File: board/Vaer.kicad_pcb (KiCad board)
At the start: 2 copper layers, 84.4 x 84.4 mm, 36 parts, among them J1 USB_C_Receptacle, U1 ESP32-S3-WROOM-1, U2 NCP1117-3.3_SOT223, U3 BQ24073RGT, U4 BME280

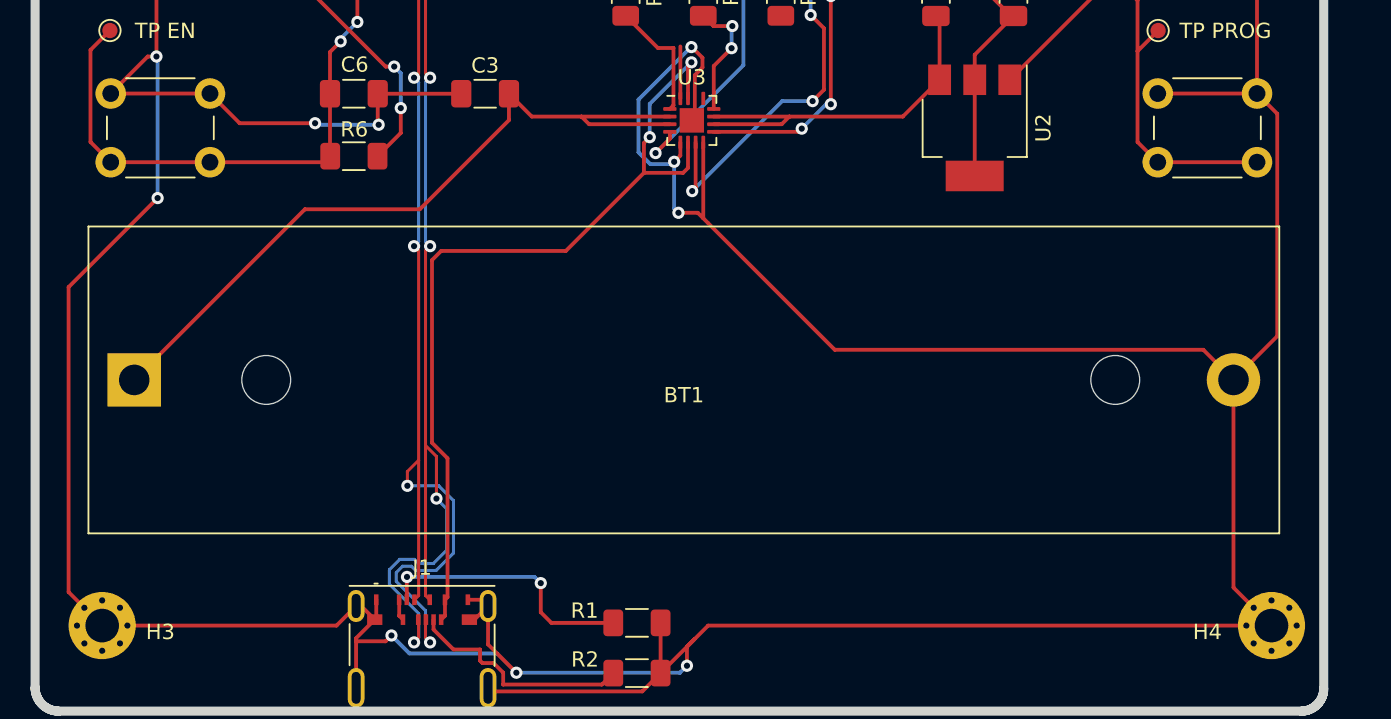
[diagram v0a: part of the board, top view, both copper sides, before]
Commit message: :recycle: Change the battery holder
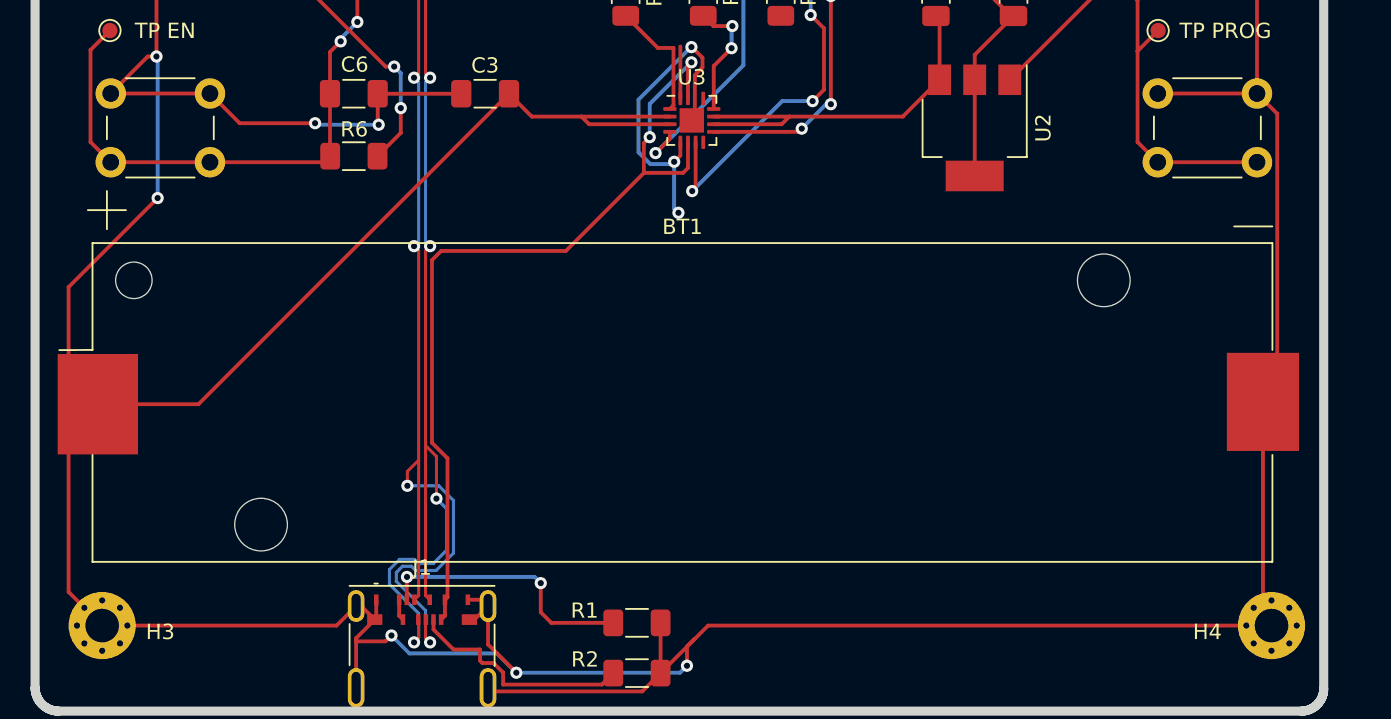
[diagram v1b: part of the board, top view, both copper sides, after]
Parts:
- BT1: footprint Battery:BatteryHolder_MPD_BH-18650-PC2 -> Battery:BatteryHolder_Keystone_1042_1x18650
- moved BT1 35.9 mm to (146.0, 113.2)
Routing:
- net GND: track 538.7 -> 491.2 mm
- net Net-(BT1-+): track 50.5 -> 52.5 mm

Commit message: :beers: Add code laying around locally :/
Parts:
- H1, H4: footprint MountingHole:MountingHole_2.2mm_M2_Pad_Via -> MountingHole:MountingHole_2.5mm_Pad_Via
- moved U4 183.8 mm to (282.9, 159.2)
- moved TP6 181.0 mm to (274.2, 161.7)
- moved TP1 174.3 mm to (268.1, 158.6)
- moved TP2 173.4 mm to (268.1, 161.7)
- moved TP3 171.8 mm to (271.1, 158.6)
- moved TP4 170.9 mm to (271.1, 161.7)
- moved C1 151.5 mm to (234.8, 158.8)
- moved SW_RESET1 151.1 mm to (239.8, 167.7)
- moved C2 150.5 mm to (234.8, 162.1)
- moved U3 146.9 mm to (278.3, 159.7)
- moved C6 137.8 mm to (234.8, 175.5), turned to 0 degrees
- moved D3 135.5 mm to (257.9, 176.1), turned to 0 degrees
- moved D2 128.7 mm to (257.9, 172.7), turned to 0 degrees
- moved U2 128.4 mm to (259.8, 181.9), turned to 0 degrees
- moved C3 124.9 mm to (234.8, 165.5)
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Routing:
- net GND: track 491.2 -> 0.00 mm, vias 10 -> 0
- net VCC_ESP: track 161.7 -> 0.00 mm, vias 8 -> 0
- net D+: track 80.6 -> 0.00 mm, vias 4 -> 0
- net D-: track 80.0 -> 0.64 mm, vias 6 -> 0
- net EN: track 75.6 -> 0.00 mm, vias 2 -> 0
- net ~{CE}: track 61.1 -> 0.00 mm, vias 4 -> 0
- net VCC_EBUS: track 57.5 -> 0.00 mm, vias 2 -> 0
- net PROG: track 52.7 -> 0.00 mm, vias 4 -> 0
- net Net-(BT1-+): track 52.5 -> 0.00 mm
- net ~{CHG}: track 48.0 -> 0.00 mm, vias 6 -> 0
- net ~{PGOOD}: track 44.4 -> 0.00 mm, vias 4 -> 0
- net MISO: track 41.8 -> 0.00 mm, vias 4 -> 0
- net MOSI: track 36.8 -> 0.00 mm, vias 2 -> 0
- net SCLK: track 34.4 -> 0.00 mm, vias 2 -> 0
- net CS: track 32.3 -> 0.00 mm, vias 4 -> 0
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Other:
- board text removed: "Humidity Pressure Temperature"
- board text removed: "PWR"
- board text removed: "TP CLK"
- board text removed: "TP CS"
- board text removed: "TP EN"
- board text removed: "TP MISO"
- board text removed: "TP MOSI"
- board text removed: "TP PROG"
- board text removed: "locked"
- board text removed: "~{CHG}"
- board text removed: "~{PGOOD}"

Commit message: :construction: Layed out the PCB again
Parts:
- moved U2 175.5 mm to (123.3, 71.5)
- moved SW_RESET1 165.3 mm to (117.0, 57.0)
- moved C6 158.6 mm to (129.4, 57.0)
- moved U3 158.4 mm to (135.2, 92.0), turned to 90 degrees
- moved C5 157.7 mm to (109.4, 76.5), turned to 180 degrees
- moved C2 157.4 mm to (109.4, 67.0)
- moved C1 152.7 mm to (109.5, 71.5)
- moved U4 141.5 mm to (158.5, 91.7), turned to 90 degrees
- moved D1 137.4 mm to (165.0, 68.0)
- moved D2 137.0 mm to (165.0, 72.0)
- moved D3 136.6 mm to (165.0, 76.0)
- moved C4 129.9 mm to (130.1, 92.0), turned to -90 degrees
- moved SW_FLASH1 127.3 mm to (163.8, 57.0)
- moved R1 118.8 mm to (114.5, 85.5), turned to 180 degrees
- moved R8 118.8 mm to (135.1, 88.0), turned to 180 degrees
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
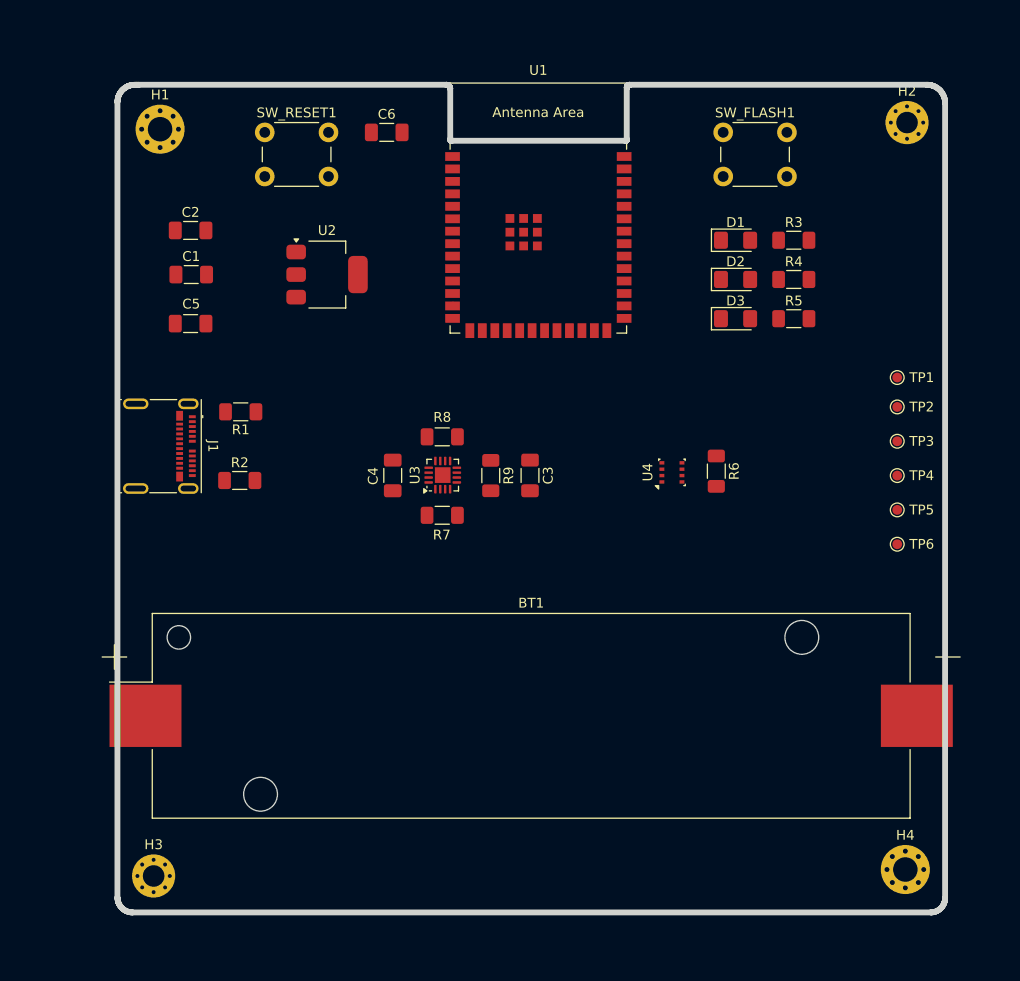
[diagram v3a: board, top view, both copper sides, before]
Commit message: :sparkles: Rerouted all components
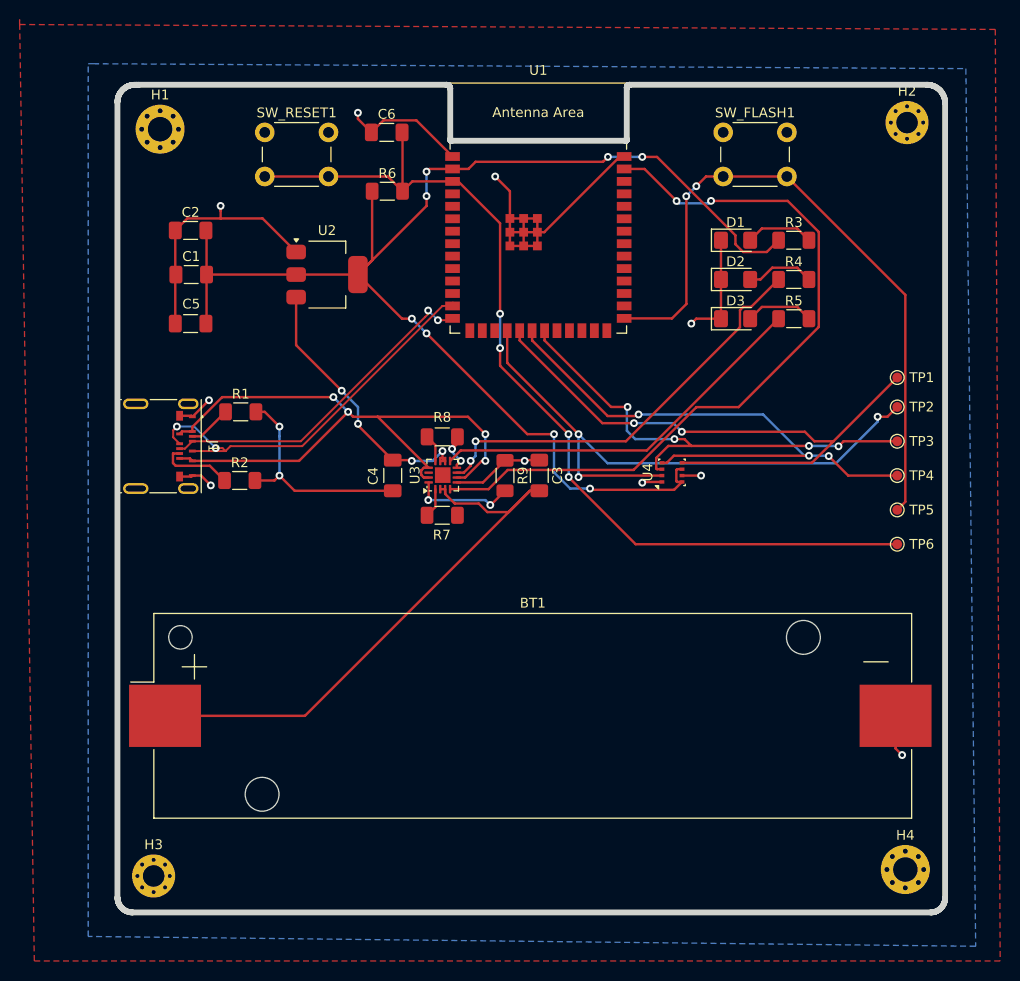
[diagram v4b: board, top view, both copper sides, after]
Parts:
- moved R6 44.1 mm to (129.5, 63.0), turned to 0 degrees
- moved R9 1.45 mm to (141.5, 92.0)
- moved C3 0.95 mm to (145.0, 92.0)
- moved BT1 0.16 mm to (144.3, 116.5)
- turned R1 to 0 degrees
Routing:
- net VCC_ESP: track 0.00 -> 136.3 mm, vias 0 -> 8
- net GND: track 0.00 -> 134.8 mm, vias 0 -> 14
- net EN: track 0.00 -> 98.0 mm, vias 0 -> 4
- net ~{CE}: track 0.00 -> 76.9 mm, vias 0 -> 2
- net VCC_EBUS: track 0.00 -> 69.8 mm, vias 0 -> 4
- net PROG: track 0.00 -> 68.4 mm, vias 0 -> 2
- net CS: track 0.00 -> 62.9 mm, vias 0 -> 3
- net MISO: track 0.00 -> 62.8 mm, vias 0 -> 2
- net SCLK: track 0.00 -> 59.4 mm, vias 0 -> 3
- net Net-(BT1-+): track 0.00 -> 59.0 mm
- net MOSI: track 0.00 -> 48.9 mm, vias 0 -> 4
- net ~{CHG}: track 0.00 -> 43.2 mm, vias 0 -> 2
- net D-: track 0.64 -> 41.5 mm, vias 0 -> 2
- net ~{PGOOD}: track 0.00 -> 39.5 mm
- net D+: track 0.00 -> 34.4 mm, vias 0 -> 2
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- added copper zone on F.Cu, net (none)
- added copper zone on B.Cu, net GND

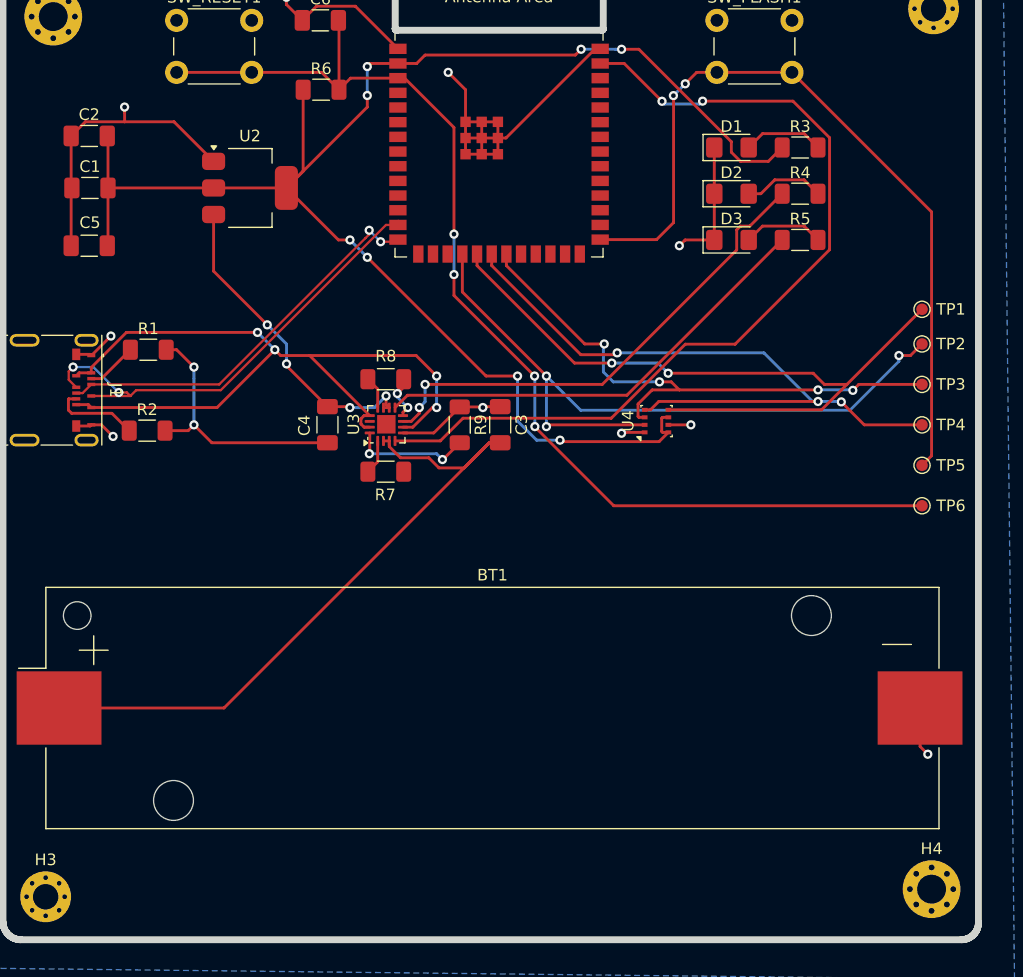
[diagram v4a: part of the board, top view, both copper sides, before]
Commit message: :sparkles: Add some missing board markings
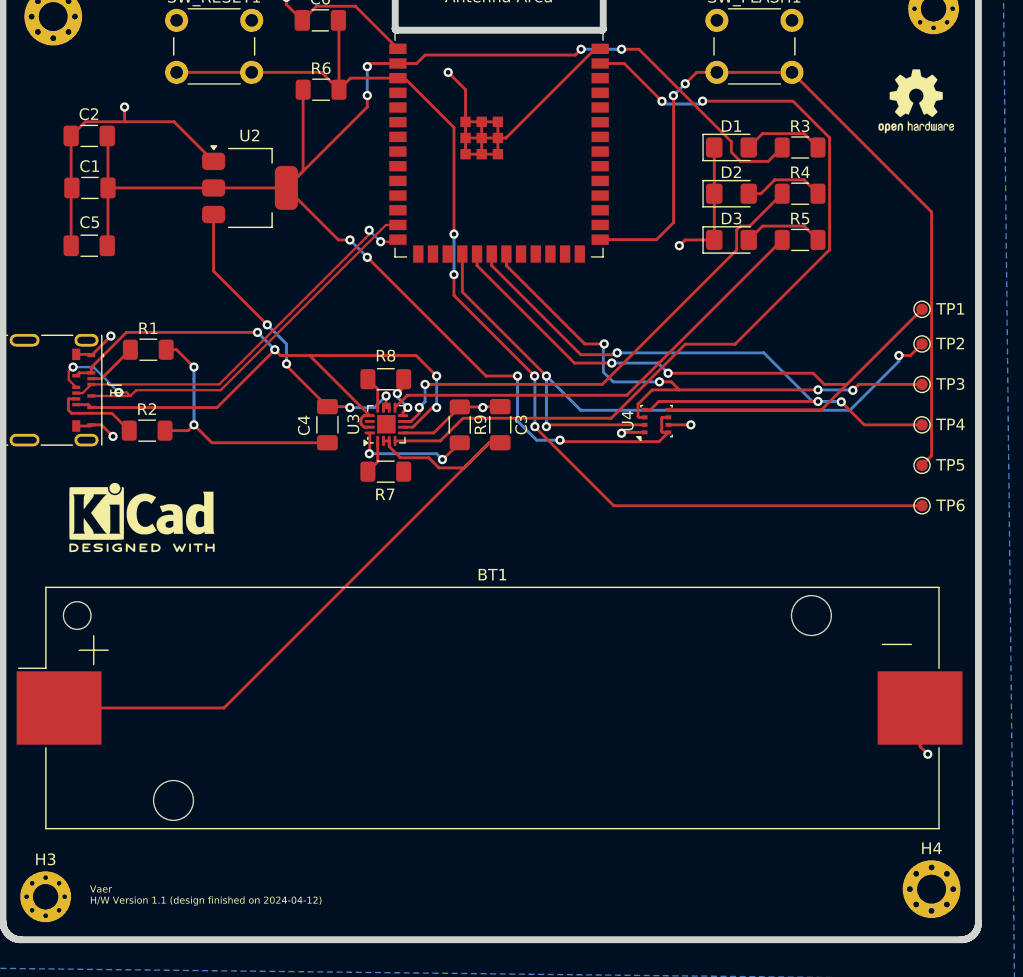
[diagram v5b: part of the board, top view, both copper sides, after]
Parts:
- added REF**: OSHW-Logo2_7.3x6mm_SilkScreen, Symbol:OSHW-Logo2_7.3x6mm_SilkScreen, F.Cu at (181.0, 64.0)
- added REF**: KiCad-Logo2_5mm_SilkScreen, Symbol:KiCad-Logo2_5mm_SilkScreen, F.Cu at (114.0, 100.0)
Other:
- board text added: "Vaer H/W Version ${REVISION} (design finished on ${ISSUE_DATE})"

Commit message: :fire: Remove the current PCB design to start over
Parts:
- removed BT1: Battery_Cell, Battery:BatteryHolder_Keystone_1042_1x18650
- removed C1, C2: 100nF, Capacitor_SMD:C_1206_3216Metric_Pad1.33x1.80mm_HandSolder
- removed C3: 4.7uF, Capacitor_SMD:C_1206_3216Metric_Pad1.33x1.80mm_HandSolder
- removed C4, C5: 10uF, Capacitor_SMD:C_1206_3216Metric_Pad1.33x1.80mm_HandSolder
- removed C6: 1uF, Capacitor_SMD:C_1206_3216Metric_Pad1.33x1.80mm_HandSolder
- removed D1: LED_BLUE_PWR, LED_SMD:LED_1206_3216Metric_Pad1.42x1.75mm_HandSolder
- removed D2: LED_YELLOW, LED_SMD:LED_1206_3216Metric_Pad1.42x1.75mm_HandSolder
- removed D3: LED_GREEN, LED_SMD:LED_1206_3216Metric_Pad1.42x1.75mm_HandSolder
- removed H1, H4: MountingHole_Pad, MountingHole:MountingHole_2.5mm_Pad_Via
- removed H2, H3: MountingHole_Pad, MountingHole:MountingHole_2.2mm_M2_Pad_Via
- removed J1: USB_C_Receptacle, Connector_USB:USB_C_Receptacle_Molex_105450-0101
- removed R1, R2: 5k1, Resistor_SMD:R_1206_3216Metric_Pad1.30x1.75mm_HandSolder
- removed R3: 120, Resistor_SMD:R_1206_3216Metric_Pad1.30x1.75mm_HandSolder
- removed R4, R5: 1k5, Resistor_SMD:R_1206_3216Metric_Pad1.30x1.75mm_HandSolder
- removed R6, R7: 10k, Resistor_SMD:R_1206_3216Metric_Pad1.30x1.75mm_HandSolder
- removed R8: 1k18, Resistor_SMD:R_1206_3216Metric_Pad1.30x1.75mm_HandSolder
- removed R9: 1k13, Resistor_SMD:R_1206_3216Metric_Pad1.30x1.75mm_HandSolder
- removed REF**: OSHW-Logo2_7.3x6mm_SilkScreen, Symbol:OSHW-Logo2_7.3x6mm_SilkScreen
- removed REF**: KiCad-Logo2_5mm_SilkScreen, Symbol:KiCad-Logo2_5mm_SilkScreen
- removed SW_FLASH1: Flash mode, Button_Switch_THT:SW_PUSH_6mm
- removed SW_RESET1: Reset, Button_Switch_THT:SW_PUSH_6mm
- removed TP1, TP2, TP3, TP4, TP5, TP6: TestPoint, TestPoint:TestPoint_Pad_D1.0mm
- removed U1: ESP32-S3-WROOM-1, Espressif:ESP32-S3-WROOM-1
- removed U2: NCP1117-3.3_SOT223, Package_TO_SOT_SMD:SOT-223-3_TabPin2
- removed U3: BQ24073RGT, Package_DFN_QFN:VQFN-16-1EP_3x3mm_P0.5mm_EP1.6x1.6mm
- removed U4: BME280, Package_LGA:Bosch_LGA-8_2.5x2.5mm_P0.65mm_ClockwisePinNumbering
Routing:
- net VCC_ESP: track 136.3 -> 0.00 mm, vias 8 -> 0
- net GND: track 134.8 -> 0.00 mm, vias 14 -> 0
- net EN: track 98.0 -> 0.00 mm, vias 4 -> 0
- net ~{CE}: track 76.9 -> 0.00 mm, vias 2 -> 0
- net VCC_EBUS: track 69.8 -> 0.00 mm, vias 4 -> 0
- net PROG: track 68.4 -> 0.00 mm, vias 2 -> 0
- net CS: track 62.9 -> 0.00 mm, vias 3 -> 0
- net MISO: track 62.8 -> 0.00 mm, vias 2 -> 0
- net SCLK: track 59.4 -> 0.00 mm, vias 3 -> 0
- net Net-(BT1-+): track 59.0 -> 0.00 mm
- net MOSI: track 48.9 -> 0.00 mm, vias 4 -> 0
- net ~{CHG}: track 43.2 -> 0.00 mm, vias 2 -> 0
- net D-: track 41.5 -> 0.00 mm, vias 2 -> 0
- net ~{PGOOD}: track 39.5 -> 0.00 mm
- net D+: track 34.4 -> 0.00 mm, vias 2 -> 0
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- removed copper zone on F.Cu, net (none)
- removed copper zone on B.Cu, net GND
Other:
- board outline removed
- board text removed: "Vaer H/W Version ${REVISION} (design finished on ${ISSUE_DATE})"
